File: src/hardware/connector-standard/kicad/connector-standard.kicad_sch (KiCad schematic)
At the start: 2 parts, among them J1 ESC Connector, J2 UART Connector

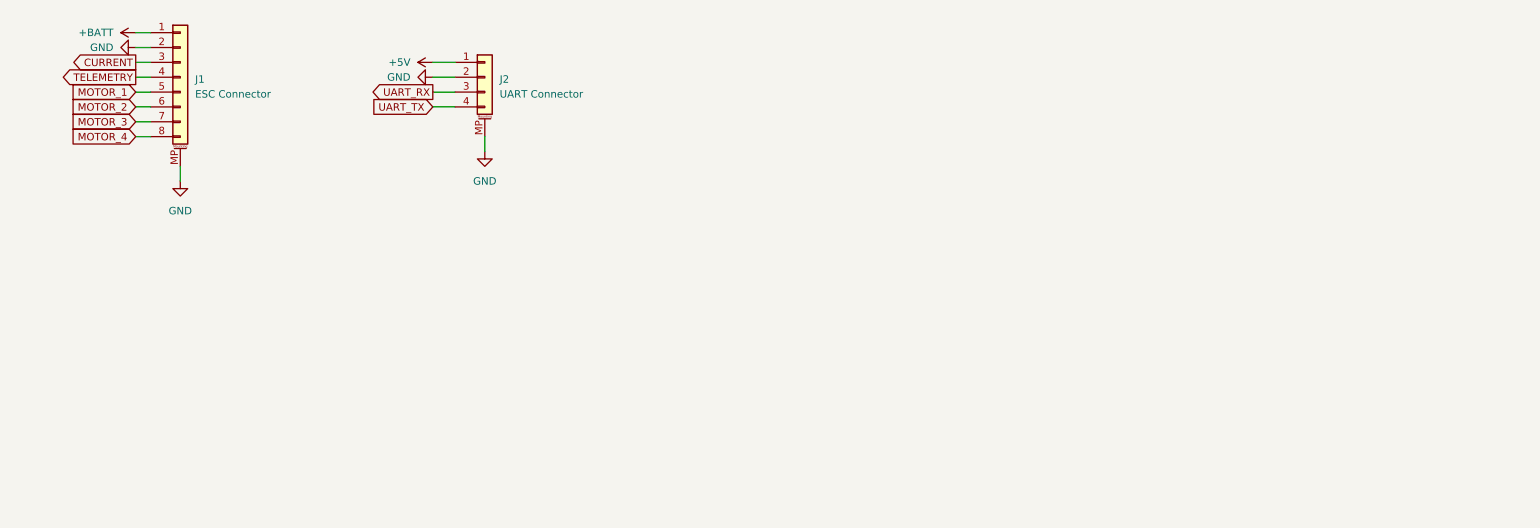
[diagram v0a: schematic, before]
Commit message: Hardware: Re-implement all existing connectors
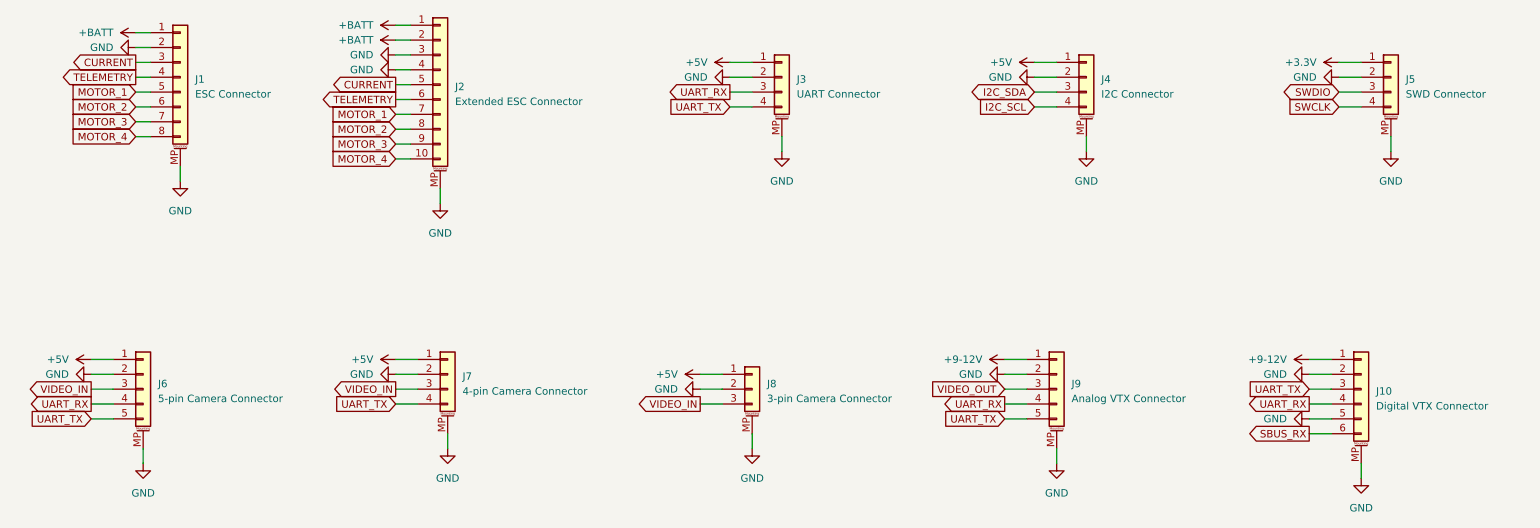
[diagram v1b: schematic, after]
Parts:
- removed J2: UART Connector, Connector_JST:JST_SH_SM04B-SRSS-TB_1x04-1MP_P1.00mm_Horizontal, symbol Connector_Generic_MountingPin:Conn_01x04_MountingPin
- added J10: Digital VTX Connector, Connector_JST:JST_SH_SM06B-SRSS-TB_1x06-1MP_P1.00mm_Horizontal, symbol Connector_Generic_MountingPin:Conn_01x06_MountingPin
- added J2: Extended ESC Connector, Connector_JST:JST_SH_SM10B-SRSS-TB_1x10-1MP_P1.00mm_Horizontal, symbol Connector_Generic_MountingPin:Conn_01x10_MountingPin
- added J3: UART Connector, Connector_JST:JST_SH_SM04B-SRSS-TB_1x04-1MP_P1.00mm_Horizontal, symbol Connector_Generic_MountingPin:Conn_01x04_MountingPin
- added J4: I2C Connector, Connector_JST:JST_SH_SM04B-SRSS-TB_1x04-1MP_P1.00mm_Horizontal, symbol Connector_Generic_MountingPin:Conn_01x04_MountingPin
- added J5: SWD Connector, Connector_JST:JST_SH_SM04B-SRSS-TB_1x04-1MP_P1.00mm_Horizontal, symbol Connector_Generic_MountingPin:Conn_01x04_MountingPin
- added J6: 5-pin Camera Connector, Connector_JST:JST_SH_SM05B-SRSS-TB_1x05-1MP_P1.00mm_Horizontal, symbol Connector_Generic_MountingPin:Conn_01x05_MountingPin
- added J7: 4-pin Camera Connector, Connector_JST:JST_SH_SM04B-SRSS-TB_1x04-1MP_P1.00mm_Horizontal, symbol Connector_Generic_MountingPin:Conn_01x04_MountingPin
- added J8: 3-pin Camera Connector, Connector_JST:JST_SH_SM03B-SRSS-TB_1x03-1MP_P1.00mm_Horizontal, symbol Connector_Generic_MountingPin:Conn_01x03_MountingPin
- added J9: Analog VTX Connector, Connector_JST:JST_SH_SM05B-SRSS-TB_1x05-1MP_P1.00mm_Horizontal, symbol Connector_Generic_MountingPin:Conn_01x05_MountingPin
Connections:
- net +5V: now also J3.1 (Pin_1), J4.1 (Pin_1), J6.1 (Pin_1), J7.1 (Pin_1), J8.1 (Pin_1)
- net +BATT: now also J2.1 (Pin_1), J2.2 (Pin_2)
- net CURRENT: now also J2.5 (Pin_5)
- net GND: now also J10.2 (Pin_2), J10.5 (Pin_5), J10.MP (MountPin), J2.3 (Pin_3), J2.4 (Pin_4), J2.MP (MountPin), J3.2 (Pin_2), J3.MP (MountPin), J4.2 (Pin_2), J4.MP (MountPin), J5.2 (Pin_2), J5.MP (MountPin), J6.2 (Pin_2), J6.MP (MountPin), J7.2 (Pin_2), J7.MP (MountPin), J8.2 (Pin_2), J8.MP (MountPin), J9.2 (Pin_2), J9.MP (MountPin)
- net MOTOR_1: now also J2.7 (Pin_7)
- net MOTOR_2: now also J2.8 (Pin_8)
- net MOTOR_3: now also J2.9 (Pin_9)
- net MOTOR_4: now also J2.10 (Pin_10)
- net TELEMETRY: now also J2.6 (Pin_6)
- net UART_RX: now also J10.4 (Pin_4), J3.3 (Pin_3), J6.4 (Pin_4), J9.4 (Pin_4)
- net UART_TX: now also J10.3 (Pin_3), J3.4 (Pin_4), J6.5 (Pin_5), J7.4 (Pin_4), J9.5 (Pin_5)
- new net +3.3V: J5.1 (Pin_1)
- new net +9-12V: J10.1 (Pin_1), J9.1 (Pin_1)
- new net I2C_SCL: J4.4 (Pin_4)
- new net I2C_SDA: J4.3 (Pin_3)
- new net SBUS_RX: J10.6 (Pin_6)
- new net SWCLK: J5.4 (Pin_4)
- new net SWDIO: J5.3 (Pin_3)
- new net VIDEO_IN: J6.3 (Pin_3), J7.3 (Pin_3), J8.3 (Pin_3)
- new net VIDEO_OUT: J9.3 (Pin_3)
